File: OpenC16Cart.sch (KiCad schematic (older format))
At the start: 13 parts, among them CN1 C16_EXP_PORT_44PIN, J1 Conn_02x03_Odd_Even, J2 Conn_02x03_Odd_Even, U1 27512

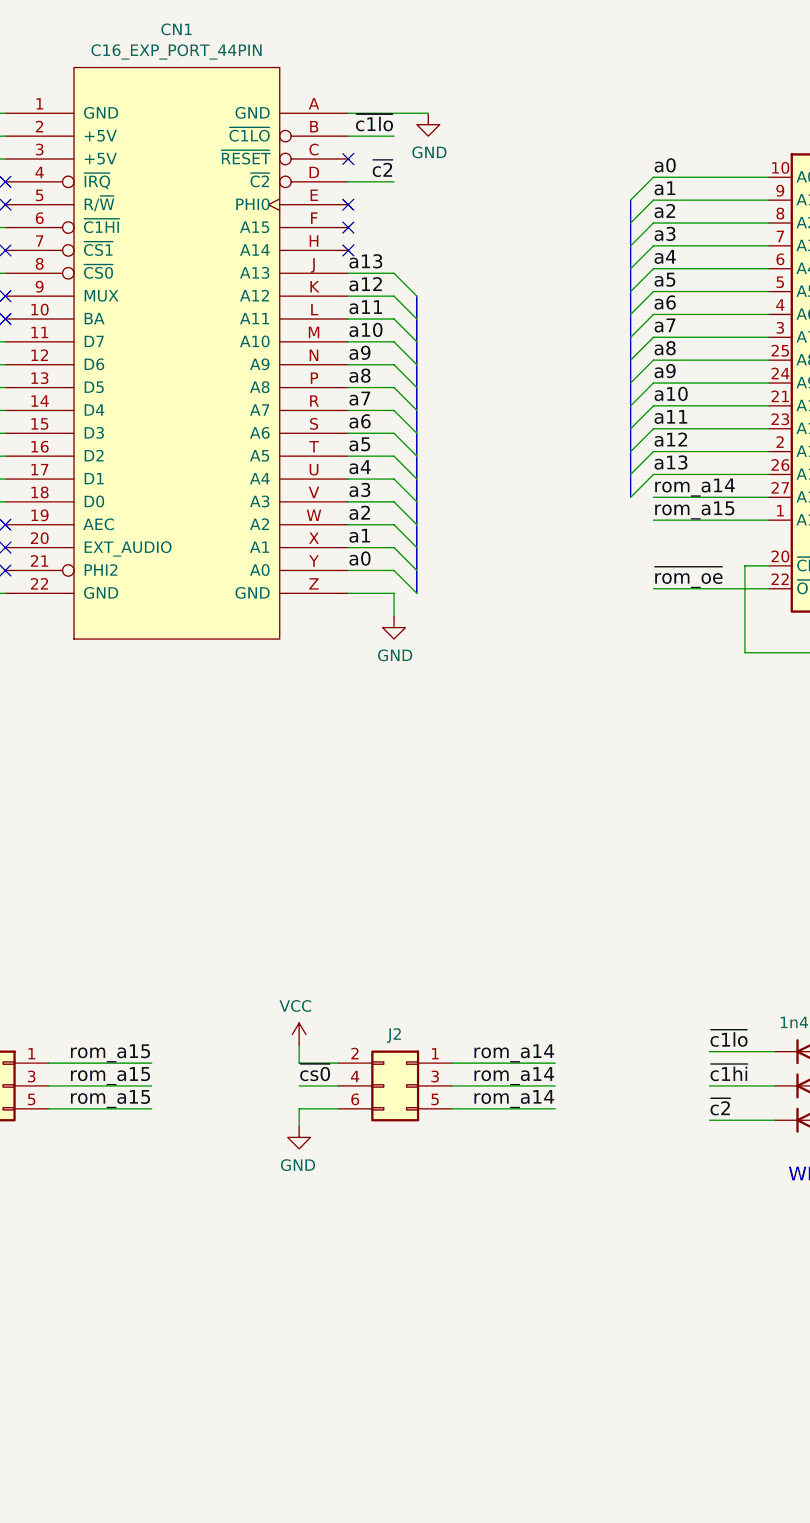
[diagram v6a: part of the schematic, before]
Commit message: Add reset button
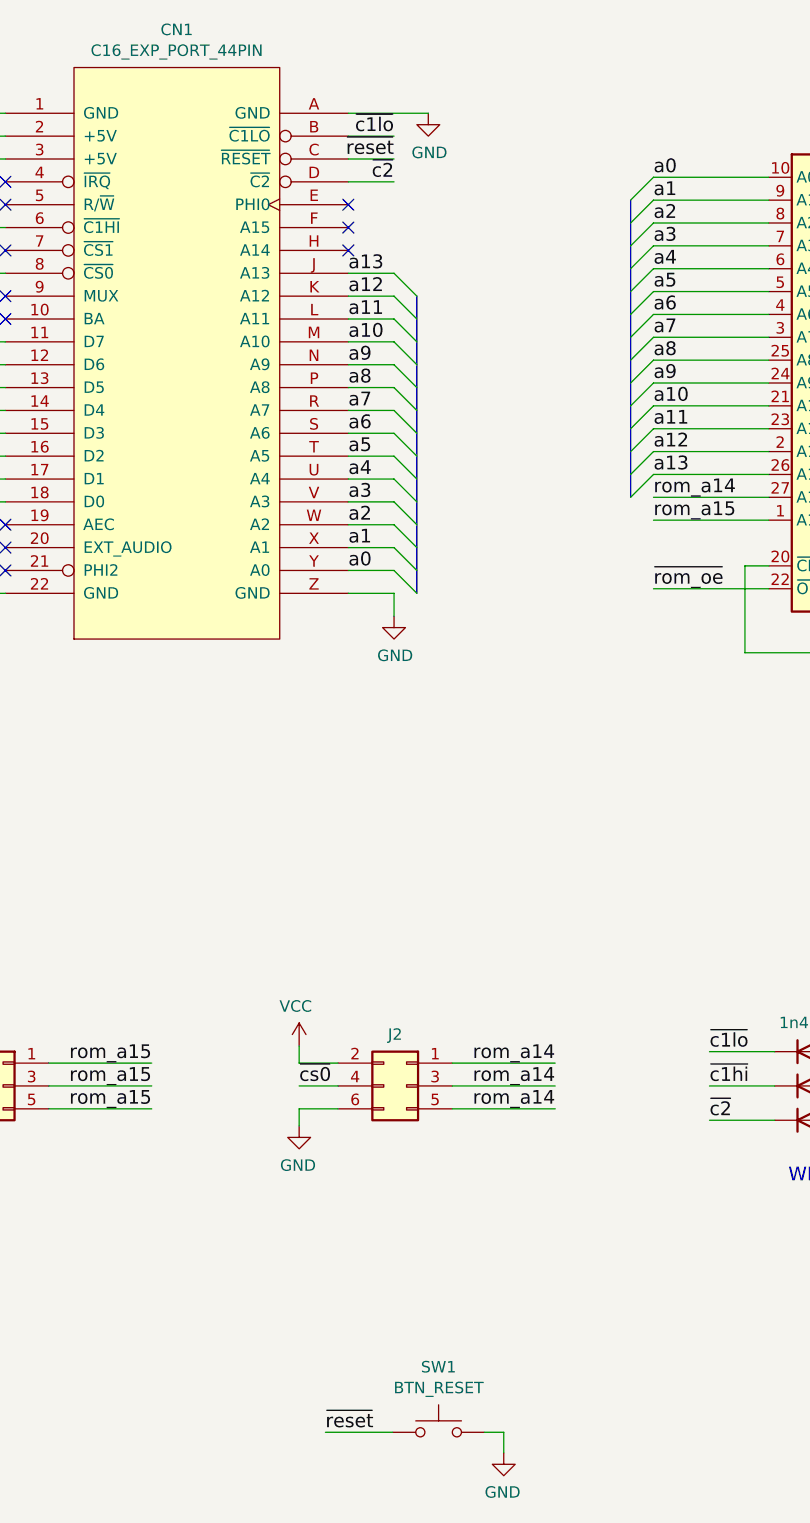
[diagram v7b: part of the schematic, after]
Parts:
- added SW1: BTN_RESET, Button_Switch_THT:SW_PUSH_6mm_H8mm, symbol Switch:SW_Push
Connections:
- net GND: now also SW1.2
- net ~reset: now reaches CN1.C (~RESET)
- net ~reset: now also SW1.1
- no-connect marks 12 -> 11
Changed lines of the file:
@@
 NoConn ~ 1655 2075
 NoConn ~ 1655 2175
-NoConn ~ 3155 1475
 NoConn ~ 3155 1675
 Entry Wire Line
@@
 Text Label 4735 5530 0    60   ~ 0
 ~c1hi
+$Comp
+L void:Void V2
+U 1 1 652D5807
+P 9955 6375
+F 0 "V2" H 10033 6421 50  0000 L CNN
+F 1 "LOGO2" H 10033 6330 50  0000 L CNN
+F 2 "OpenC16Cart:logo2" H 9955 6375 50  0001 C CNN
+F 3 "" H 9955 6375 50  0001 C CNN
+	1    9955 6375
+	1    0    0    -1
+$EndComp
+$Comp
+L void:Void V1
+U 1 1 652D5F22
+P 9955 6125
+F 0 "V1" H 10033 6171 50  0000 L CNN
+F 1 "LOGO1" H 10033 6080 50  0000 L CNN
+F 2 "OpenC16Cart:logo1" H 9955 6125 50  0001 C CNN
+F 3 "" H 9955 6125 50  0001 C CNN
+	1    9955 6125
+	1    0    0    -1
+$EndComp
+$Comp
+L Switch:SW_Push SW1
+U 1 1 66884D32
+P 3550 7045
+F 0 "SW1" H 3550 7330 50  0000 C CNN
+F 1 "BTN_RESET" H 3550 7239 50  0000 C CNN
+F 2 "Button_Switch_THT:SW_PUSH_6mm_H8mm" H 3550 7245 50  0001 C CNN
+F 3 "~" H 3550 7245 50  0001 C CNN
+	1    3550 7045
+	1    0    0    -1
+$EndComp
+Wire Wire Line
+	3750 7045 3835 7045
+Wire Wire Line
+	3835 7045 3835 7135
+$Comp
+L power:GND #PWR0103
+U 1 1 66889CBF
+P 3835 7135
+F 0 "#PWR0103" H 3835 6885 50  0001 C CNN
+F 1 "GND" H 3840 6962 50  0000 C CNN
+F 2 "" H 3835 7135 50  0001 C CNN
+F 3 "" H 3835 7135 50  0001 C CNN
+	1    3835 7135
+	-1   0    0    -1
+$EndComp
+Wire Wire Line
+	3155 1475 3355 1475
+Text Label 3355 1475 2    60   ~ 0
+~reset
+Text Label 3055 7045 0    60   ~ 0
+~reset
+Wire Wire Line
+	3350 7045 3055 7045
 Wire Bus Line
 	6250 1455 6250 2155
@@
 Wire Bus Line
 	4390 1655 4390 2955
-$Comp
-L void:Void V2
-U 1 1 652D5807
-P 9955 6375
-F 0 "V2" H 10033 6421 50  0000 L CNN
-F 1 "LOGO2" H 10033 6330 50  0000 L CNN
-F 2 "OpenC16Cart:logo2" H 9955 6375 50  0001 C CNN
-F 3 "" H 9955 6375 50  0001 C CNN
-	1    9955 6375
-	1    0    0    -1
-$EndComp
-$Comp
-L void:Void V1
-U 1 1 652D5F22
-P 9955 6125
-F 0 "V1" H 10033 6171 50  0000 L CNN
-F 1 "LOGO1" H 10033 6080 50  0000 L CNN
-F 2 "OpenC16Cart:logo1" H 9955 6125 50  0001 C CNN
-F 3 "" H 9955 6125 50  0001 C CNN
-	1    9955 6125
-	1    0    0    -1
-$EndComp
 $EndSCHEMATC

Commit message: Make hole compliant with Stumpy cases
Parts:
- H1: footprint MountingHole:MountingHole_3.2mm_M3 -> MountingHole:MountingHole_5mm
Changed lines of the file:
@@
 F 0 "H1" H 10665 6161 50  0000 L CNN
 F 1 "MountingHole" H 10665 6070 50  0000 L CNN
-F 2 "MountingHole:MountingHole_3.2mm_M3" H 10565 6115 50  0001 C CNN
+F 2 "MountingHole:MountingHole_5mm" H 10565 6115 50  0001 C CNN
 F 3 "~" H 10565 6115 50  0001 C CNN
 	1    10565 6115
